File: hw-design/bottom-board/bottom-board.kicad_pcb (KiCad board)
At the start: 2 copper layers, 172 x 140.5 mm, 256 parts, among them J1 JACK_TRS_6PINS, J2 JACK_TRS_6PINS, J3 JACK_TRS_6PINS, J4 JACK_TRS_6PINS, J5 JACK_TRS_6PINS, J6 RJ45_LEDS, J7 Conn_02x50_Odd_Even, J8 Conn_02x50_Odd_Even, K1 IM06TS, K2 IM06TS, P1 USB_B, P2 USB_A, P3 DIN_5, P4 DIN_5, P5 BARREL_JACK, P6 HMI_POWER, P8 HMI_DATA, P9 SERIAL_DEBUG, Q1 2N7002, Q10 2N7002, Q12 2N7002, Q13 2N7002, Q14 BSS84, Q15 BSS84, Q2 2N7002, Q3 J112, Q4 J112, Q5 J112, Q6 J112, Q7 2N7002, Q8 2N7002, Q9 2N7002, SW1 SW_PUSH, U1 MURATA 5V, U10 RT9742MNGJ5, U11 6N137S, U12 ISL83491, U13 AP2120N-3.3, U2 LD1117S50TR_SOT223, U3 CS4245, U4 AT24CS08-STUM, U6 LM4562, U7 LM4562, U8 LM4562, U9 LM4811

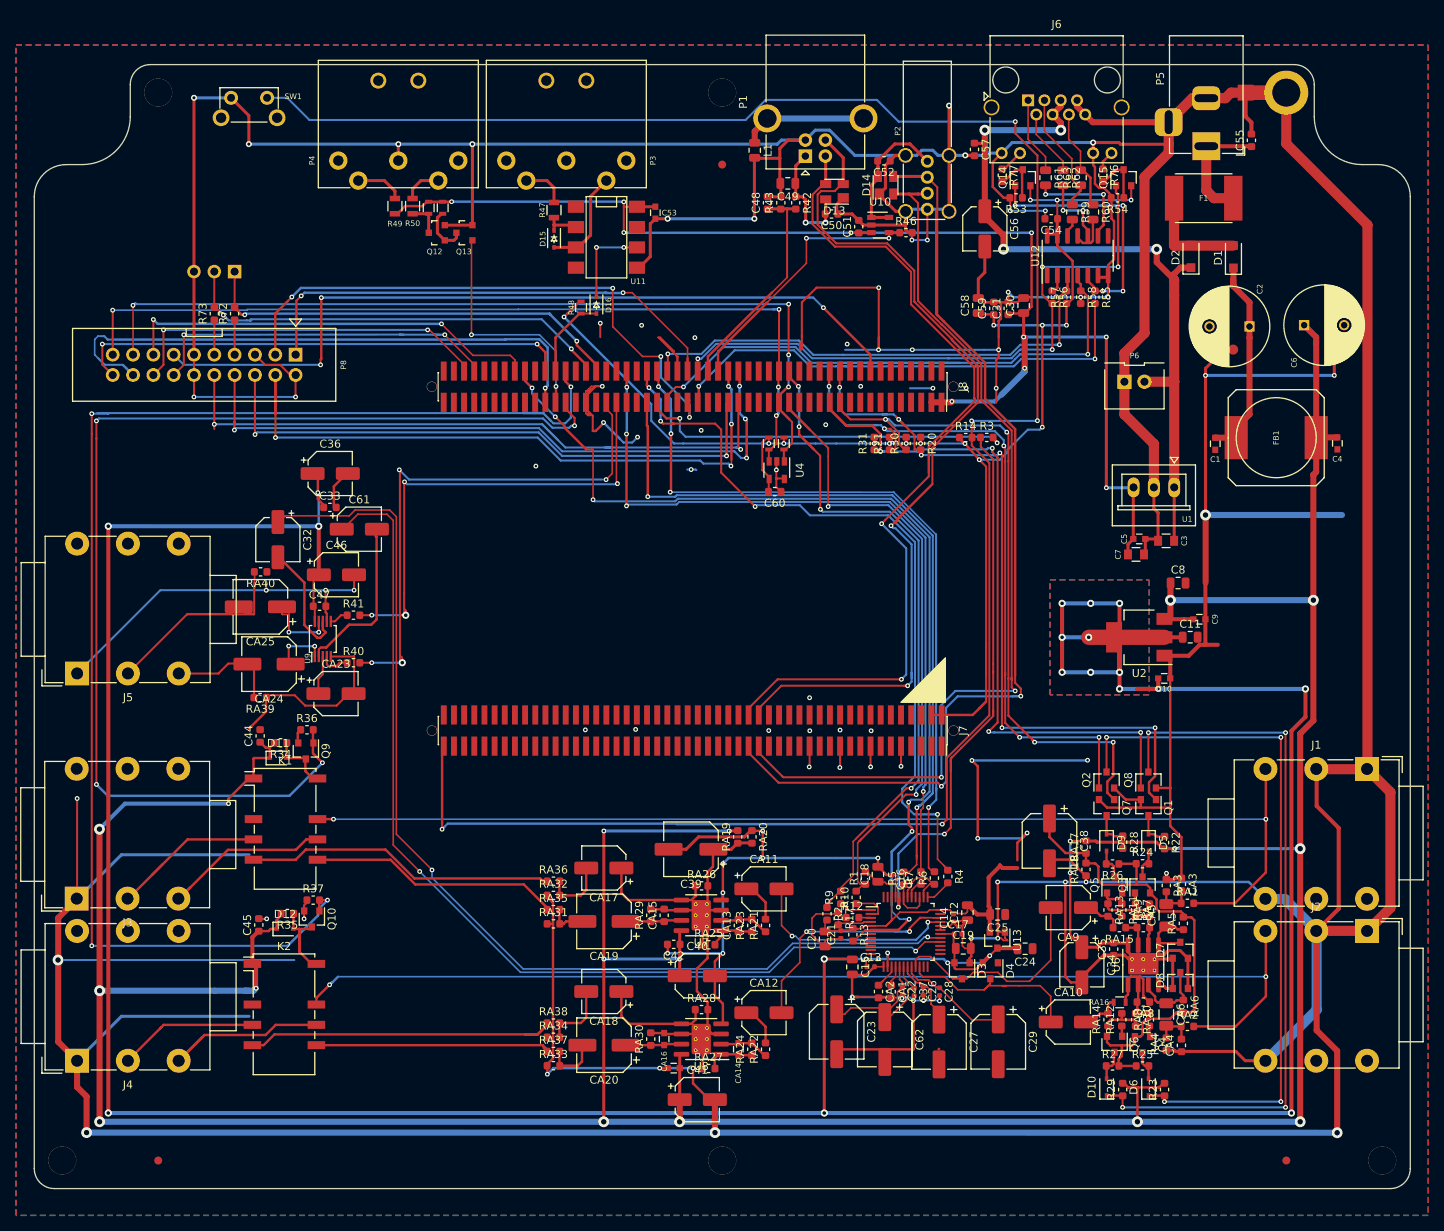
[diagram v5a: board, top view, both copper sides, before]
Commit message: correct tracks that overlap with new footprints
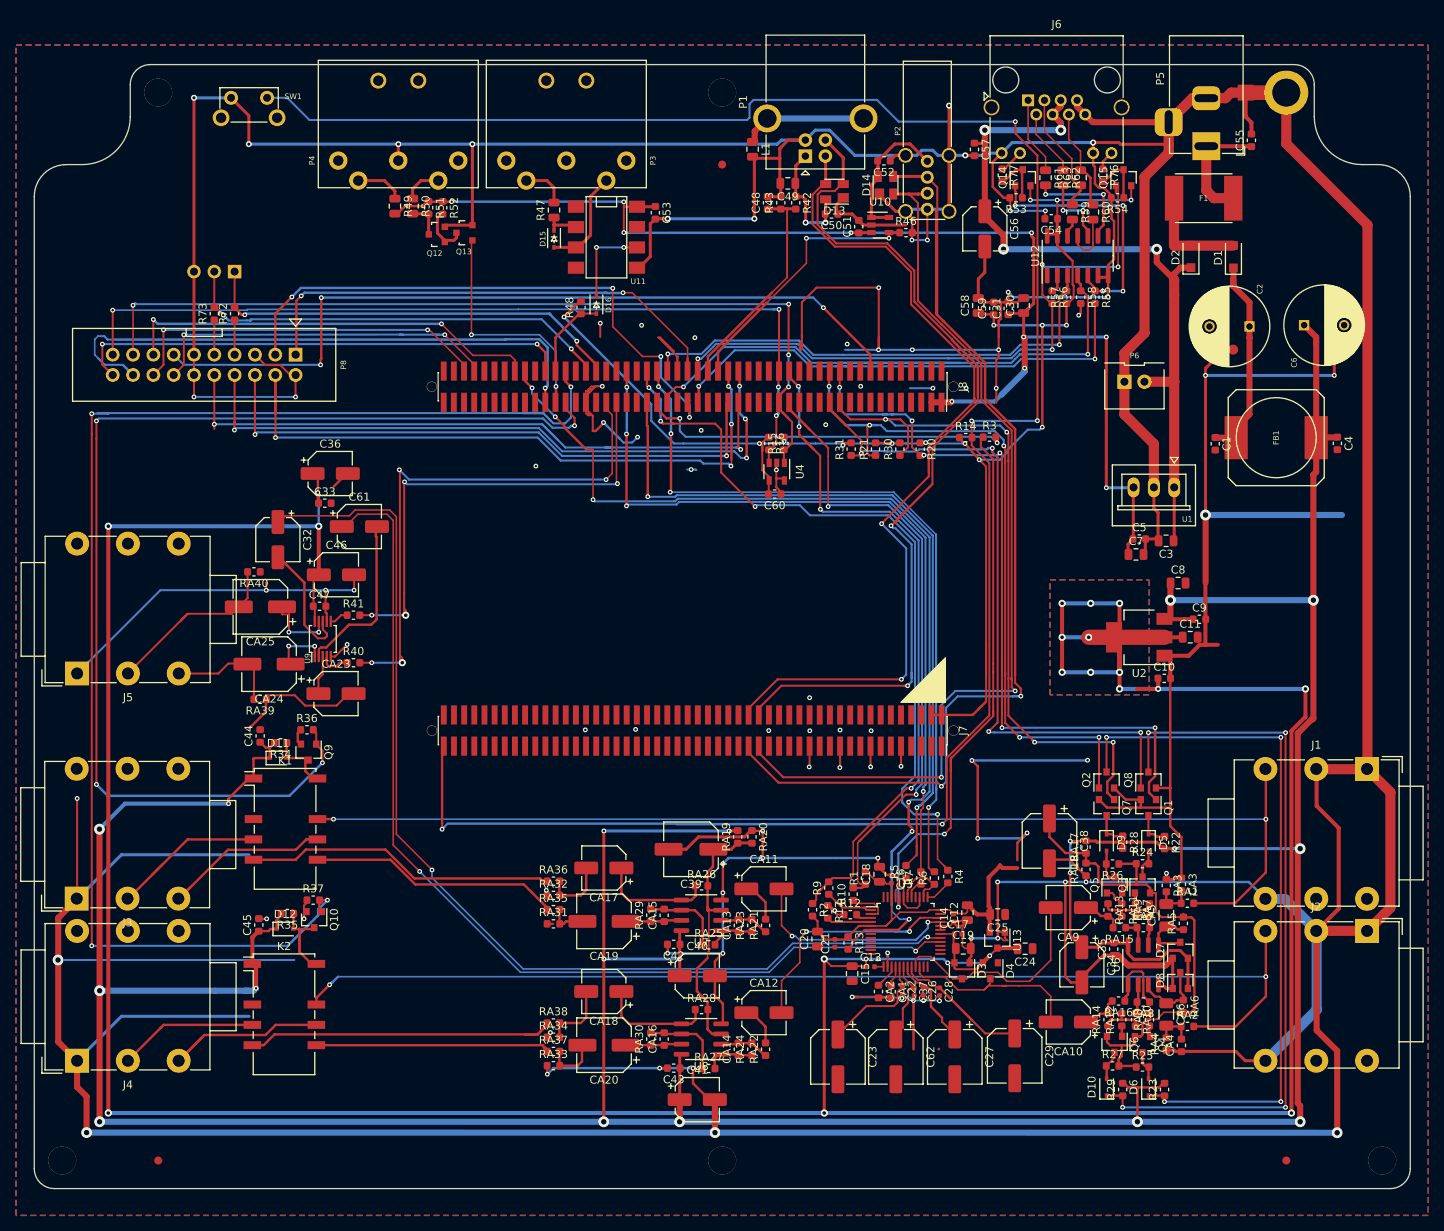
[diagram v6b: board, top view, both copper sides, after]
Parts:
- removed G***: LOGO, footprints:mod-logo
- C1, C10, C4, C43, C5, C53, C9, CA14, CA16: footprint Capacitors_SMD:C_0603 -> Capacitor_SMD:C_0603_1608Metric
- C3, C7: footprint Capacitors_SMD:C_0805 -> Capacitor_SMD:C_0805_2012Metric
- R15, R16, R48, R51, R52, RA16: footprint Resistors_SMD:R_0603 -> Resistor_SMD:R_0603_1608Metric
- R47, R49, R50: footprint Resistors_SMD:R_0805 -> Resistor_SMD:R_0805_2012Metric
- U6, U7, U8: footprint Package_SO:SOIC-8-1EP_3.9x4.9mm_P1.27mm_EP2.41x3.81mm_ThermalVias -> Package_SO:SOIC-8_3.9x4.9mm_P1.27mm
- moved C23 3.14 mm to (160.5, 143.6)
- moved R31 2.98 mm to (162.2, 67.6)
- moved C27 2.71 mm to (175.1, 143.6)
- moved C29 2.70 mm to (182.6, 143.5)
- moved C62 2.57 mm to (167.8, 143.6)
- moved R9 1.90 mm to (159.4, 122.5)
- moved R21 1.89 mm to (165.2, 67.6)
- moved R2 1.87 mm to (157.4, 125.2)
- moved R17 1.55 mm to (159.3, 125.5)
- moved C21 1.33 mm to (160.1, 129.4)
- moved R13 1.18 mm to (161.8, 129.4)
- moved R30 1.06 mm to (168.3, 67.6)
- moved C20 0.93 mm to (158.0, 128.9)
- moved R5 0.85 mm to (169.0, 120.5)
- moved RA40 0.84 mm to (87.5, 83.0)
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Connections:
- J1 pad RN: Net-(J1-PadRN) -> (no net)
- J1 pad SN: Net-(J1-PadSN) -> (no net)
- J2 pad RN: Net-(J2-PadRN) -> (no net)
- J2 pad SN: Net-(J2-PadSN) -> (no net)
- J3 pad RN: Net-(J3-PadRN) -> (no net)
- J3 pad SN: Net-(J3-PadSN) -> (no net)
- J3 pad TN: Net-(J3-PadTN) -> (no net)
- J4 pad RN: Net-(J4-PadRN) -> (no net)
- J4 pad SN: Net-(J4-PadSN) -> (no net)
- J4 pad TN: Net-(J4-PadTN) -> (no net)
- J5 pad RN: Net-(J5-PadRN) -> (no net)
- J5 pad SN: Net-(J5-PadSN) -> (no net)
- J5 pad TN: Net-(J5-PadTN) -> (no net)
- J7 pad 100: Net-(J7-Pad100) -> (no net)
- J7 pad 11: Net-(J7-Pad11) -> (no net)
- J7 pad 12: Net-(J7-Pad12) -> (no net)
- J7 pad 13: Net-(J7-Pad13) -> (no net)
- J7 pad 14: Net-(J7-Pad14) -> (no net)
- J7 pad 17: Net-(J7-Pad17) -> (no net)
- J7 pad 18: Net-(J7-Pad18) -> (no net)
- J7 pad 19: Net-(J7-Pad19) -> (no net)
- J7 pad 20: Net-(J7-Pad20) -> (no net)
- J7 pad 23: Net-(J7-Pad23) -> (no net)
- J7 pad 24: Net-(J7-Pad24) -> (no net)
- J7 pad 25: Net-(J7-Pad25) -> (no net)
- J7 pad 26: Net-(J7-Pad26) -> (no net)
- J7 pad 29: Net-(J7-Pad29) -> (no net)
- J7 pad 30: Net-(J7-Pad30) -> (no net)
- J7 pad 31: Net-(J7-Pad31) -> (no net)
- J7 pad 32: Net-(J7-Pad32) -> (no net)
- J7 pad 33: Net-(J7-Pad33) -> (no net)
- J7 pad 34: Net-(J7-Pad34) -> (no net)
- J7 pad 42: Net-(J7-Pad42) -> (no net)
- J7 pad 43: Net-(J7-Pad43) -> (no net)
- J7 pad 44: Net-(J7-Pad44) -> (no net)
- J7 pad 45: Net-(J7-Pad45) -> (no net)
- J7 pad 46: Net-(J7-Pad46) -> (no net)
- J7 pad 48: Net-(J7-Pad48) -> (no net)
- J7 pad 49: Net-(J7-Pad49) -> (no net)
- J7 pad 5: Net-(J7-Pad5) -> (no net)
- J7 pad 50: Net-(J7-Pad50) -> (no net)
- J7 pad 51: Net-(J7-Pad51) -> (no net)
- J7 pad 52: Net-(J7-Pad52) -> (no net)
- J7 pad 53: Net-(J7-Pad53) -> (no net)
- J7 pad 54: Net-(J7-Pad54) -> (no net)
- J7 pad 55: Net-(J7-Pad55) -> (no net)
- J7 pad 56: Net-(J7-Pad56) -> (no net)
- J7 pad 57: Net-(J7-Pad57) -> (no net)
- J7 pad 58: Net-(J7-Pad58) -> (no net)
- J7 pad 59: Net-(J7-Pad59) -> (no net)
- J7 pad 6: Net-(J7-Pad6) -> (no net)
- J7 pad 60: Net-(J7-Pad60) -> (no net)
- J7 pad 63: Net-(J7-Pad63) -> (no net)
- J7 pad 64: Net-(J7-Pad64) -> (no net)
- J7 pad 65: Net-(J7-Pad65) -> (no net)
- J7 pad 66: Net-(J7-Pad66) -> (no net)
- J7 pad 67: Net-(J7-Pad67) -> (no net)
- J7 pad 68: Net-(J7-Pad68) -> (no net)
- J7 pad 69: Net-(J7-Pad69) -> (no net)
- J7 pad 7: Net-(J7-Pad7) -> (no net)
- J7 pad 70: Net-(J7-Pad70) -> (no net)
- J7 pad 71: Net-(J7-Pad71) -> (no net)
- J7 pad 73: Net-(J7-Pad73) -> (no net)
- J7 pad 74: Net-(J7-Pad74) -> (no net)
- J7 pad 75: Net-(J7-Pad75) -> (no net)
- J7 pad 76: Net-(J7-Pad76) -> (no net)
- J7 pad 77: Net-(J7-Pad77) -> (no net)
- J7 pad 78: Net-(J7-Pad78) -> (no net)
- J7 pad 79: Net-(J7-Pad79) -> (no net)
- J7 pad 8: Net-(J7-Pad8) -> (no net)
- J7 pad 80: Net-(J7-Pad80) -> (no net)
- J7 pad 81: Net-(J7-Pad81) -> (no net)
- J7 pad 82: Net-(J7-Pad82) -> (no net)
- J7 pad 83: Net-(J7-Pad83) -> (no net)
- J7 pad 84: Net-(J7-Pad84) -> (no net)
- J7 pad 85: Net-(J7-Pad85) -> (no net)
- J7 pad 86: Net-(J7-Pad86) -> (no net)
- J7 pad 87: Net-(J7-Pad87) -> (no net)
- J7 pad 88: Net-(J7-Pad88) -> (no net)
- J7 pad 89: Net-(J7-Pad89) -> (no net)
- J7 pad 90: Net-(J7-Pad90) -> (no net)
- J7 pad 91: Net-(J7-Pad91) -> (no net)
- J7 pad 92: Net-(J7-Pad92) -> (no net)
- J7 pad 93: Net-(J7-Pad93) -> (no net)
- J7 pad 94: Net-(J7-Pad94) -> (no net)
- J7 pad 95: Net-(J7-Pad95) -> (no net)
- J7 pad 96: Net-(J7-Pad96) -> (no net)
- J7 pad 97: Net-(J7-Pad97) -> (no net)
- J7 pad 98: Net-(J7-Pad98) -> (no net)
- J8 pad 100: Net-(J8-Pad100) -> (no net)
- J8 pad 11: Net-(J8-Pad11) -> (no net)
- J8 pad 12: Net-(J8-Pad12) -> (no net)
- J8 pad 13: Net-(J8-Pad13) -> (no net)
- J8 pad 14: Net-(J8-Pad14) -> (no net)
- J8 pad 15: Net-(J8-Pad15) -> (no net)
- J8 pad 17: Net-(J8-Pad17) -> (no net)
- J8 pad 19: Net-(J8-Pad19) -> (no net)
- J8 pad 20: Net-(J8-Pad20) -> (no net)
- J8 pad 25: Net-(J8-Pad25) -> (no net)
- J8 pad 26: Net-(J8-Pad26) -> (no net)
- J8 pad 27: Net-(J8-Pad27) -> (no net)
- J8 pad 28: Net-(J8-Pad28) -> (no net)
- J8 pad 29: Net-(J8-Pad29) -> (no net)
- J8 pad 30: Net-(J8-Pad30) -> (no net)
- J8 pad 35: Net-(J8-Pad35) -> (no net)
- J8 pad 36: Net-(J8-Pad36) -> (no net)
- J8 pad 37: Net-(J8-Pad37) -> (no net)
- J8 pad 38: Net-(J8-Pad38) -> (no net)
- J8 pad 39: Net-(J8-Pad39) -> (no net)
- J8 pad 40: Net-(J8-Pad40) -> (no net)
- J8 pad 45: Net-(J8-Pad45) -> (no net)
- J8 pad 47: Net-(J8-Pad47) -> (no net)
- J8 pad 5: Net-(J8-Pad5) -> (no net)
- J8 pad 53: Net-(J8-Pad53) -> (no net)
- J8 pad 6: Net-(J8-Pad6) -> (no net)
- J8 pad 61: Net-(J8-Pad61) -> (no net)
- J8 pad 62: Net-(J8-Pad62) -> (no net)
- J8 pad 63: Net-(J8-Pad63) -> (no net)
- J8 pad 66: Net-(J8-Pad66) -> (no net)
- J8 pad 68: Net-(J8-Pad68) -> (no net)
- J8 pad 69: Net-(J8-Pad69) -> (no net)
- J8 pad 7: Net-(J8-Pad7) -> (no net)
- J8 pad 73: Net-(J8-Pad73) -> (no net)
- J8 pad 74: Net-(J8-Pad74) -> (no net)
- J8 pad 8: Net-(J8-Pad8) -> (no net)
- J8 pad 81: Net-(J8-Pad81) -> (no net)
- J8 pad 82: Net-(J8-Pad82) -> (no net)
- J8 pad 83: Net-(J8-Pad83) -> (no net)
- J8 pad 85: Net-(J8-Pad85) -> (no net)
- J8 pad 87: Net-(J8-Pad87) -> (no net)
- J8 pad 88: Net-(J8-Pad88) -> (no net)
- J8 pad 89: Net-(J8-Pad89) -> (no net)
- J8 pad 9: Net-(J8-Pad9) -> (no net)
- J8 pad 90: Net-(J8-Pad90) -> (no net)
- J8 pad 91: Net-(J8-Pad91) -> (no net)
- J8 pad 92: Net-(J8-Pad92) -> (no net)
- J8 pad 93: Net-(J8-Pad93) -> (no net)
- J8 pad 95: Net-(J8-Pad95) -> (no net)
- J8 pad 97: Net-(J8-Pad97) -> (no net)
- J8 pad 98: Net-(J8-Pad98) -> (no net)
- J8 pad 99: Net-(J8-Pad99) -> (no net)
- P3 pad 1: Net-(P3-Pad1) -> (no net)
- P3 pad 2: Net-(P3-Pad2) -> (no net)
- P3 pad 3: Net-(P3-Pad3) -> (no net)
- P4 pad 1: Net-(P4-Pad1) -> (no net)
- P4 pad 3: Net-(P4-Pad3) -> (no net)
- U11 pad 1: Net-(U11-Pad1) -> (no net)
- U11 pad 4: Net-(U11-Pad4) -> (no net)
- U11 pad 7: Net-(U11-Pad7) -> (no net)
- U3 pad 10: Net-(U3-Pad10) -> (no net)
- U3 pad 11: Net-(U3-Pad11) -> (no net)
- U3 pad 12: Net-(U3-Pad12) -> (no net)
- U3 pad 23: Net-(U3-Pad23) -> (no net)
- U3 pad 24: Net-(U3-Pad24) -> (no net)
- U3 pad 25: Net-(U3-Pad25) -> (no net)
- U3 pad 26: Net-(U3-Pad26) -> (no net)
- U3 pad 27: Net-(U3-Pad27) -> (no net)
- U3 pad 35: Net-(U3-Pad35) -> (no net)
- U3 pad 40: Net-(U3-Pad40) -> (no net)
- U3 pad 47: Net-(U3-Pad47) -> (no net)
- U3 pad 48: Net-(U3-Pad48) -> (no net)
- U3 pad 7: Net-(U3-Pad7) -> (no net)
- U3 pad 8: Net-(U3-Pad8) -> (no net)
- U3 pad 9: Net-(U3-Pad9) -> (no net)
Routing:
- net GNDA: track 1594.6 -> 1540.4 mm, vias 87 -> 91
- net HP_RIGHT: track 33.9 -> 23.3 mm
- net Net-(C28-Pad1): track 14.2 -> 24.0 mm
- net Net-(C26-Pad1): track 8.76 -> 13.7 mm
- net +3V3: track 190.6 -> 193.8 mm, vias 16 -> 15
- net +5VA: track 471.3 -> 473.5 mm
- net LEFT_GAIN_CTRL2: track 85.9 -> 88.1 mm
- net CODEC_~RESET: track 125.5 -> 127.4 mm
- net Net-(R60-Pad2): track 5.39 -> 7.28 mm
- net Net-(CA8-Pad1): track 8.36 -> 10.2 mm
- net Net-(R9-Pad1): track 4.21 -> 6.06 mm
- net +3.3VA: track 46.4 -> 48.2 mm
- net CHAIN_UART_RX: track 78.9 -> 80.4 mm
- net Net-(R17-Pad2): track 4.26 -> 5.57 mm
- net +12VA: track 531.6 -> 533.0 mm
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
